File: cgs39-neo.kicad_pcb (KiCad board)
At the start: 2 copper layers, 65 parts, among them Q1 BC547, Q2 BC547, Q3 BC547, Q4 BC547, U1 TL074, U2 TL074

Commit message: add power & replace jacks
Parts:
- added J1: EURO_PWR_2x5, Connector_PinHeader_2.54mm:PinHeader_2x05_P2.54mm_Vertical, F.Cu at (109.2, 182.9)
- added R43: 100K, Resistor_THT:R_Axial_DIN0411_L9.9mm_D3.6mm_P15.24mm_Horizontal, F.Cu at (308.8, 163.4)
- added R44: 100K, Resistor_THT:R_Axial_DIN0411_L9.9mm_D3.6mm_P15.24mm_Horizontal, F.Cu at (308.8, 168.5)
- added R45: 100K, Resistor_THT:R_Axial_DIN0411_L9.9mm_D3.6mm_P15.24mm_Horizontal, F.Cu at (308.8, 173.7)
- added R46: 100K, Resistor_THT:R_Axial_DIN0411_L9.9mm_D3.6mm_P15.24mm_Horizontal, F.Cu at (308.8, 178.8)
- InputA1, InputA2, InputB1, InputB2, InputC1, InputC2, InputD1, InputD2, OutputA1, OutputB1, OutputC1, OutputD1: footprint Connector_Audio:Jack_6.35mm_Neutrik_NJ2FD-V_Vertical -> cgs39-neo:SIMPLE-JACK-2PIN-THT

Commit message: resistor untangle
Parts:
- moved R23 330.5 mm to (30.5, 78.7)
- moved R28 329.3 mm to (50.8, 67.9)
- moved R26 329.2 mm to (50.8, 58.4)
- moved R24 319.6 mm to (30.5, 68.6)
- moved R9 316.9 mm to (27.9, 20.3)
- moved R7 311.3 mm to (30.5, 48.3)
- moved R8 310.0 mm to (50.8, 38.1)
- moved R27 309.3 mm to (51.4, 78.7)
- moved R22 302.0 mm to (30.5, 58.4)
- moved R25 300.3 mm to (30.5, 88.9)
- moved R2 293.6 mm to (30.5, 29.2)
- moved R3 293.2 mm to (30.5, 38.1)
- moved R1 292.8 mm to (49.5, 29.2)
- moved R6 285.9 mm to (43.2, 14.6), turned to 180 degrees
- moved R29 279.6 mm to (51.4, 88.3)
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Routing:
- net GND: track 0.00 -> 40.2 mm
- net Net-(InputA1-PadT): track 0.00 -> 6.92 mm
- net Net-(R6-Pad1): track 0.00 -> 5.71 mm

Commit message: i hate this
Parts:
- R1, R10, R11, R12, R13, R14, R15, R16, R17, R18, R19, R2, R20, R21, R22, R23, R24, R25, R26, R27, R28, R29, R3, R30, R31, R32, R33, R34, R35, R36, R37, R38, R39, R4, R40, R41, R42, R43, R44, R45, R46, R5, R6, R7, R8, R9: footprint Resistor_THT:R_Axial_DIN0411_L9.9mm_D3.6mm_P15.24mm_Horizontal -> Resistor_THT:R_Axial_DIN0204_L3.6mm_D1.6mm_P5.08mm_Horizontal
- moved R14 305.5 mm to (39.1, 33.0), turned to 270 degrees
- moved R15 288.8 mm to (68.6, 26.4)
- moved R13 273.8 mm to (87.9, 26.9)
- moved R5 263.0 mm to (80.3, 25.4)
- moved R4 257.3 mm to (68.6, 3.05), turned to 270 degrees
- moved R16 252.1 mm to (84.8, 15.2)
- moved R17 247.0 mm to (89.4, 33.5), turned to 180 degrees
- moved R12 245.2 mm to (76.2, 30.5)
- moved Func1 124.0 mm to (54.4, 44.2), turned to 270 degrees
- moved U1 51.8 mm to (39.1, 29.5), turned to 90 degrees
- moved U2 47.6 mm to (43.2, 65.0)
- moved R27 24.2 mm to (27.3, 80.8)
- moved R26 23.7 mm to (27.3, 61.5)
- moved R29 23.5 mm to (27.9, 87.0)
- moved R28 23.5 mm to (27.3, 67.3)
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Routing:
- net GND: track 40.2 -> 151.1 mm
- net Net-(R10-Pad2): track 0.00 -> 34.1 mm
- net Net-(Func1-Pad1): track 0.00 -> 17.8 mm
- net Net-(R6-Pad1): track 5.71 -> 19.1 mm
- net Net-(InputA2-PadT): track 0.00 -> 6.20 mm
- net Net-(InputB1-PadT): track 0.00 -> 6.11 mm
- net Net-(InputD2-PadT): track 0.00 -> 5.82 mm
- net Net-(InputB2-PadT): track 0.00 -> 5.76 mm
- net Net-(InputD1-PadT): track 0.00 -> 5.71 mm
- net Net-(InputC1-PadT): track 0.00 -> 5.60 mm
- net Net-(R23-Pad1): track 0.00 -> 5.08 mm
- net Net-(R22-Pad1): track 0.00 -> 5.08 mm
- net Net-(R3-Pad1): track 0.00 -> 5.08 mm
- net Net-(InputC2-PadT): track 0.00 -> 5.02 mm
- net Net-(R1-Pad2): track 0.00 -> 4.06 mm
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
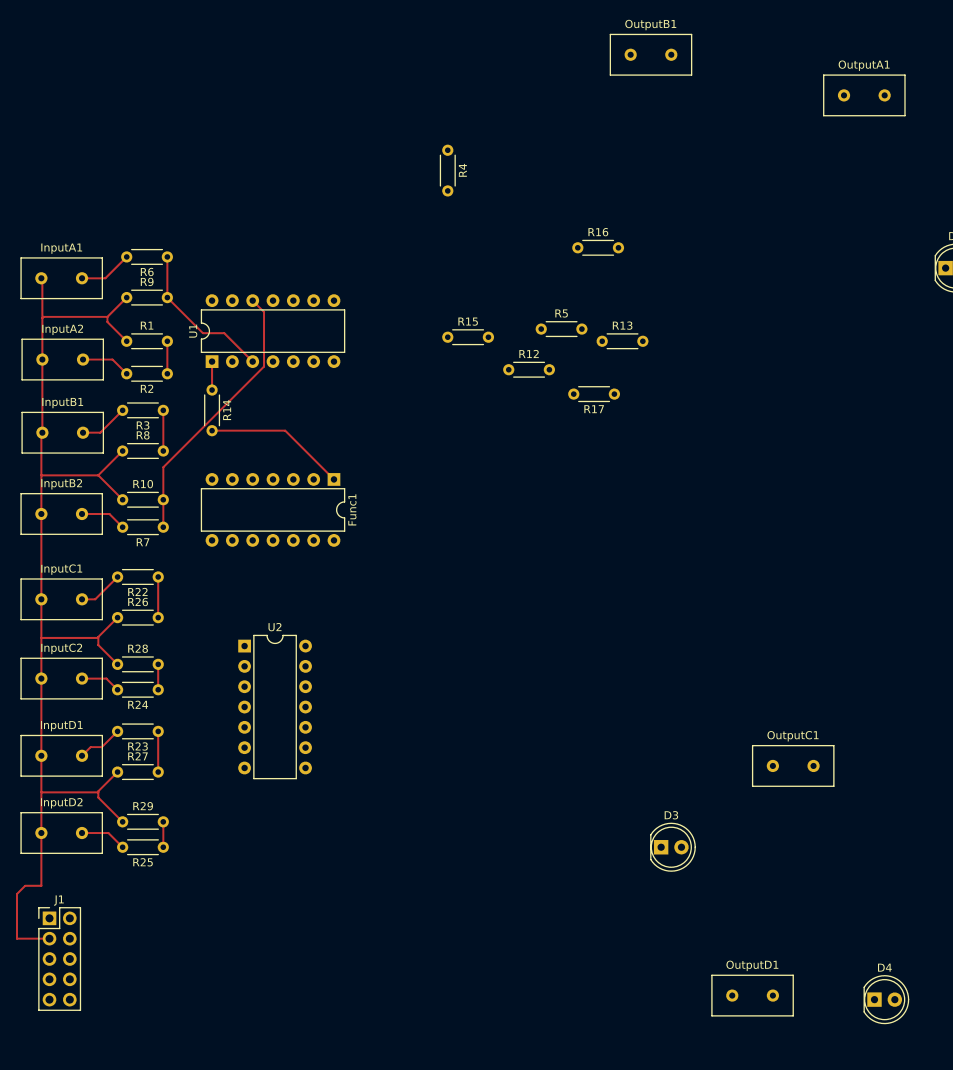
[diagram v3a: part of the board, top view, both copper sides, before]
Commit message: trying to make smoll
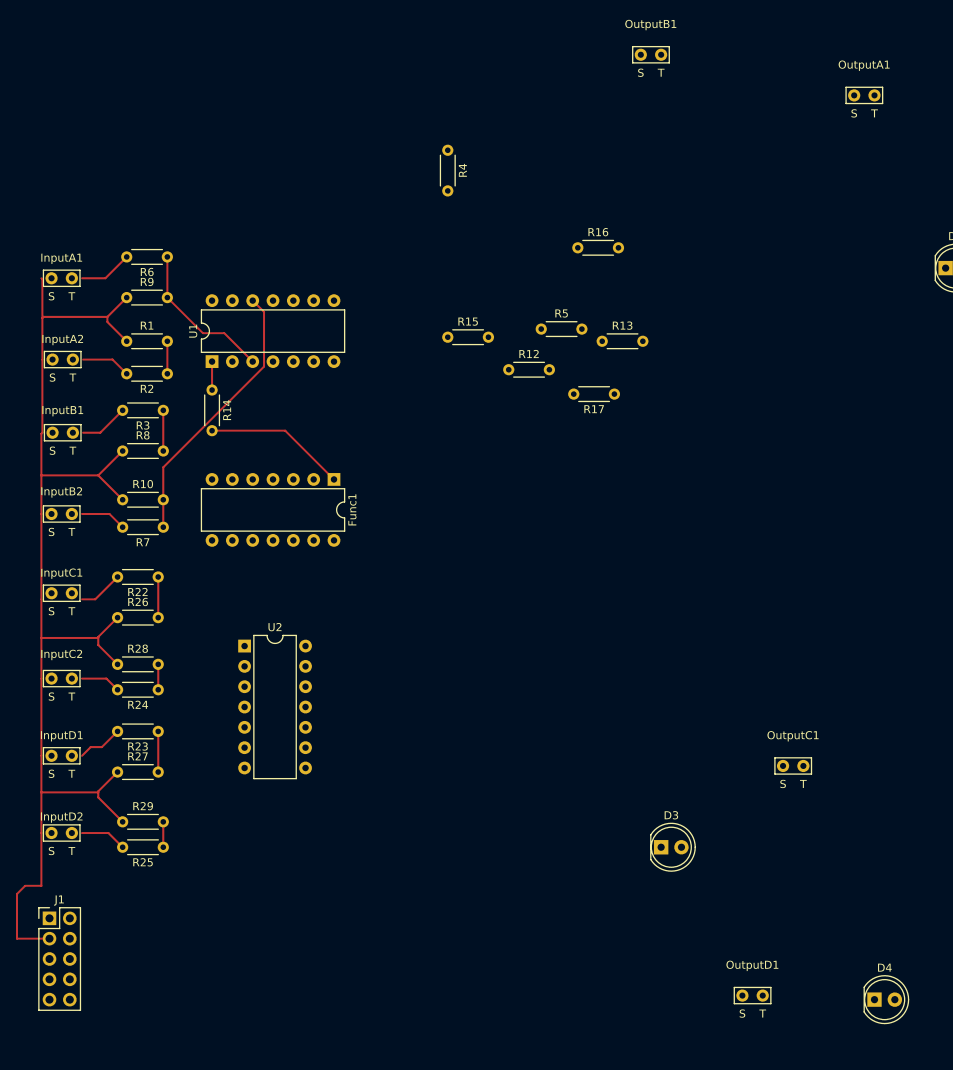
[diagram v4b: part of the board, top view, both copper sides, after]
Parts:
- moved InputC1 0.76 mm to (20.3, 58.4)

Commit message: brogres
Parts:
- moved R44 302.0 mm to (21.8, 74.4), turned to 90 degrees
- moved R34 299.7 mm to (33.0, 72.4)
- moved Q4 295.8 mm to (38.2, 122.8)
- moved Q2 295.6 mm to (38.5, 111.6)
- moved Q1 289.4 mm to (38.5, 106.0)
- moved Q3 289.1 mm to (38.5, 117.2)
- moved R35 288.5 mm to (80.8, 82.6)
- moved R19 288.5 mm to (72.4, 72.3)
- moved R21 288.5 mm to (91.6, 56.8)
- moved R32 288.5 mm to (110.8, 56.8)
- moved R33 288.5 mm to (91.6, 72.3)
- moved R36 288.5 mm to (72.4, 67.1)
- moved R42 279.1 mm to (35.4, 130.4), turned to 180 degrees
- moved R37 264.7 mm to (87.0, 56.1)
- moved R18 256.8 mm to (93.3, 82.6)
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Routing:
- net GND: track 151.1 -> 0.00 mm
- net Net-(R10-Pad2): track 34.1 -> 0.00 mm
- net Net-(R6-Pad1): track 19.1 -> 0.00 mm
- net Net-(Func1-Pad1): track 17.8 -> 0.00 mm
- net Net-(InputA1-PadT): track 6.69 -> 0.00 mm
- net Net-(InputA2-PadT): track 6.20 -> 0.00 mm
- net Net-(InputB1-PadT): track 6.11 -> 0.00 mm
- net Net-(InputD2-PadT): track 5.82 -> 0.00 mm
- net Net-(InputB2-PadT): track 5.76 -> 0.00 mm
- net Net-(InputD1-PadT): track 5.71 -> 0.00 mm
- net Net-(InputC1-PadT): track 5.60 -> 0.00 mm
- net Net-(R23-Pad1): track 5.08 -> 0.00 mm
- net Net-(R22-Pad1): track 5.08 -> 0.00 mm
- net Net-(R3-Pad1): track 5.08 -> 0.00 mm
- net Net-(InputC2-PadT): track 5.02 -> 0.00 mm
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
